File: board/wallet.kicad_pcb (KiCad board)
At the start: 4 copper layers, 48 x 85 mm, 108 parts, among them J1 TYPE-C-31-M-12, U1 BQ25185DLHR, U11 E73-2G4M08S1C, U12 ME6211C28M5G-N, U13 TPS60230RGTR, U14 TLV70313DBVR, U15 MAX17048G+T10, U2 TPS63802DLAR, U4 STM32U585VIT6Q, U5 SE050E2HQ1/Z01Z3Z, U6 TS3USB221ARSER, U7 SN74LVC1G02DBVR(UMW), U8 TPS22917DBVR, U9 TXU0202DCUR

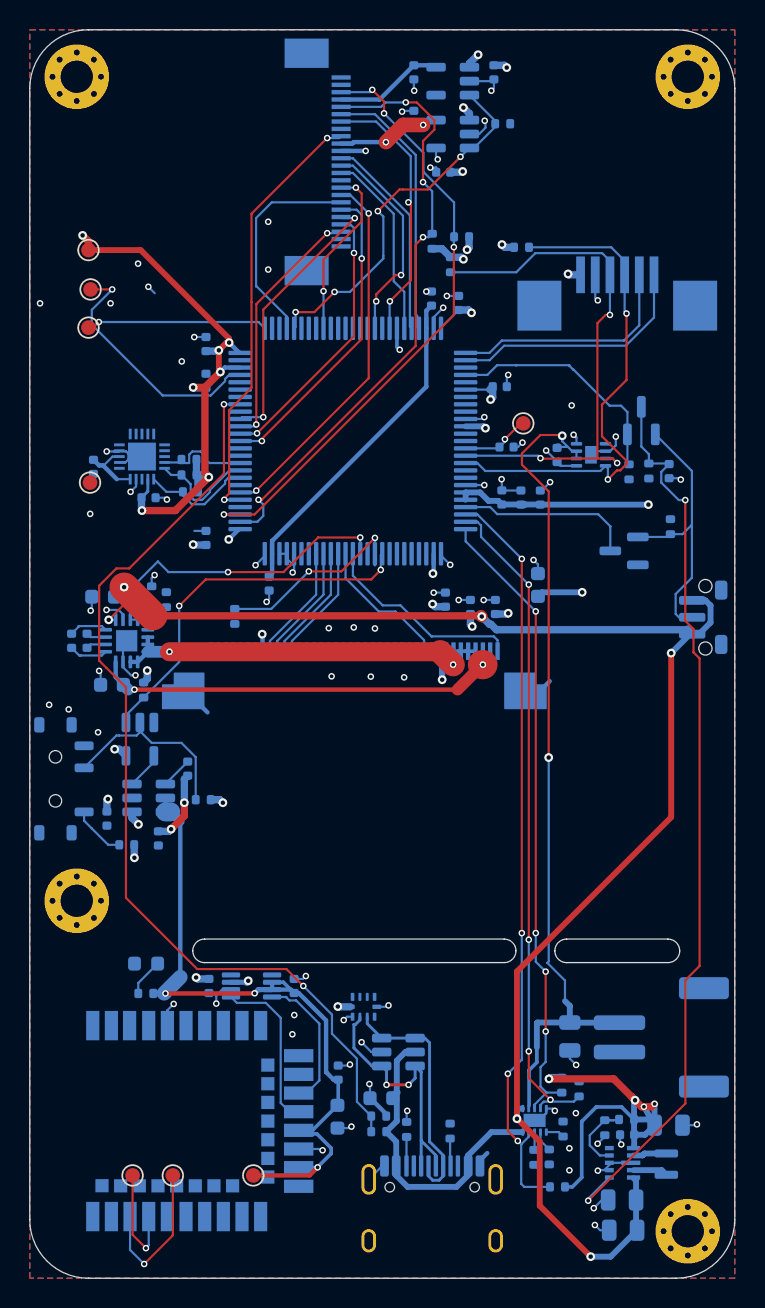
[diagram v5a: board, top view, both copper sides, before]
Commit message: Owner: radio RX routed, camera I2C pull-ups moved north, CAM_SCL re-routed
Hand work: RADIO_RXD_MCU routed (40 mm, back copper); R_CSCL moved up beside
the camera supply output (C_AVOUT turned 180 to make room), R_CSDA 1.3 mm
north, CAM_SCL redrawn to the new pull-up; small reroutes of CAM_D1, CAM_EN,
CAM_XCLK, CAM_AVDD, RADIO_3V3, V3V3, AIRGAP_SENSE; 8 GND vias.

As committed: 7 unconnected (USB MCU pair, RADIO_TXD, AIRGAP x2, J_TFT pin 40
GND now cut off from the pour), 3 vias that connect one layer only (CAM_EN,
CAM_D1, CAM_XCLK, each in the middle of a single-layer track) and 3 CAM_SCL
crumbs. Cleaned up in the next commit.

Co-Authored-By: Claude Opus 5.5 <noreply@anthropic.com>
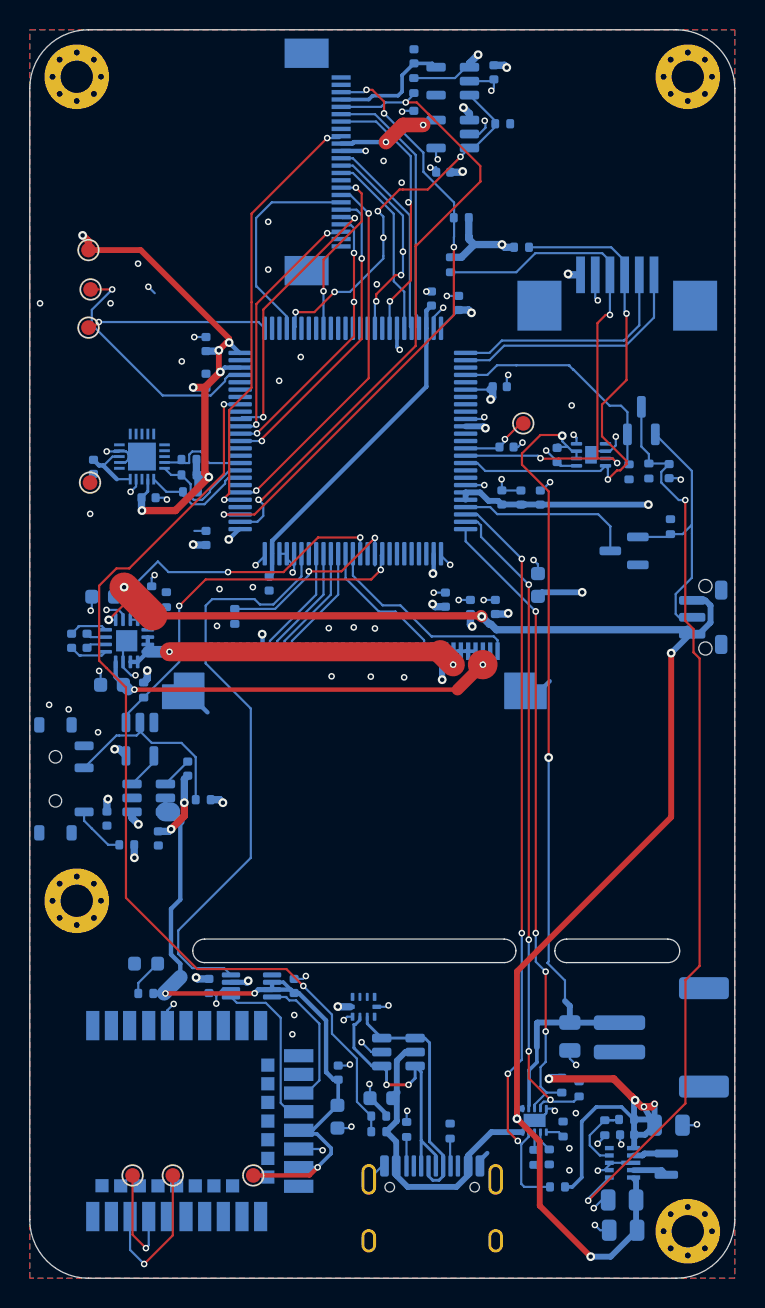
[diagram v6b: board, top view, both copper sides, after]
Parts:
- moved R_CSCL 10.7 mm to (26.1, 3.80), turned to 90 degrees
- moved R_CSDA 1.30 mm to (29.4, 12.8)
- moved C_AVOUT 1.09 mm to (26.2, 1.81), turned to 90 degrees
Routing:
- net RADIO_RXD_MCU: track 0.00 -> 40.4 mm
- net V3V3: track 128.2 -> 135.2 mm, vias 44 -> 42
- net CAM_SCL: track 41.6 -> 45.1 mm, vias 4 -> 2
- net GND: track 85.2 -> 83.5 mm, vias 80 -> 86
- net CAM_AVDD: track 7.48 -> 8.42 mm
- net RADIO_3V3: track 48.8 -> 49.3 mm
- net CAM_EN: vias 4 -> 5
- net CAM_XCLK: vias 2 -> 3
- net CAM_D1: vias 2 -> 3

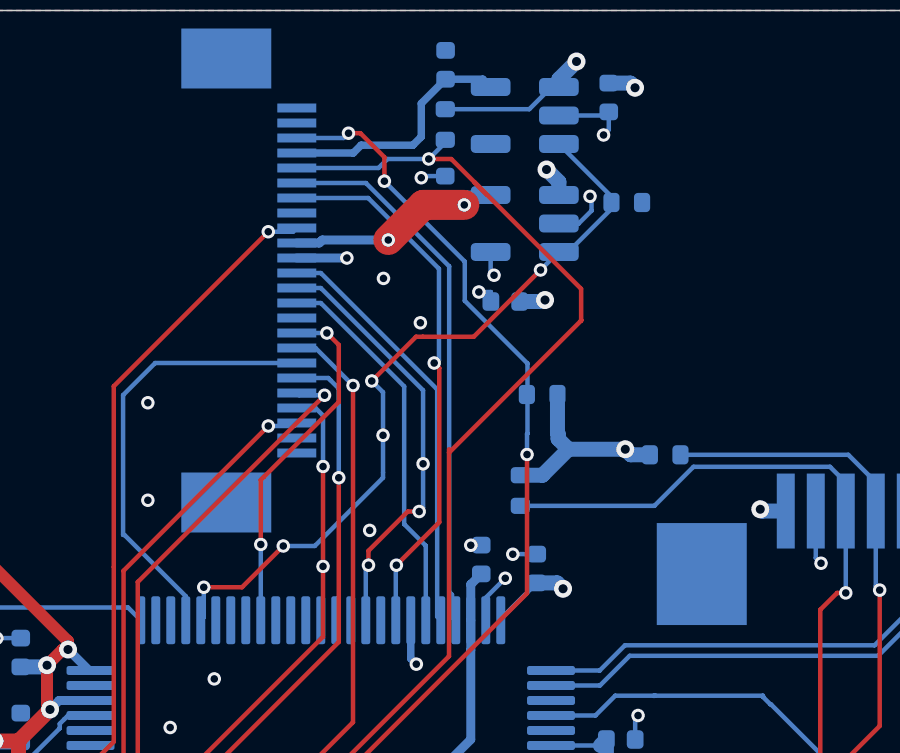
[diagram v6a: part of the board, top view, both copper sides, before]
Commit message: USB MCU pair named as a differential pair; owner's leftover vias and stubs out
USB_DP_MCU/USB_DN_MCU -> USB_MCU_DP/USB_MCU_DN: a name ending in P/N is what
KiCad's Route Differential Pair and humanRouter's pair detection both key on
(USB_DP/USB_DN already did). Renamed in the tscircuit source, the MCU and pin
maps, the net class pattern and the board; nets, AF, sync and pin-table gates pass.

cleanCopper also removes, on a net that is complete: a via that joins one
layer only (left mid-track after a reroute) and a dangling stub under 1 mm.
Nets still waiting for routing keep their fanouts. Removed: the CAM_EN, CAM_D1
and CAM_XCLK mid-track vias and three CAM_SCL stubs/crumbs; unconnected
unchanged (7).

Co-Authored-By: Claude Opus 5.5 <noreply@anthropic.com>
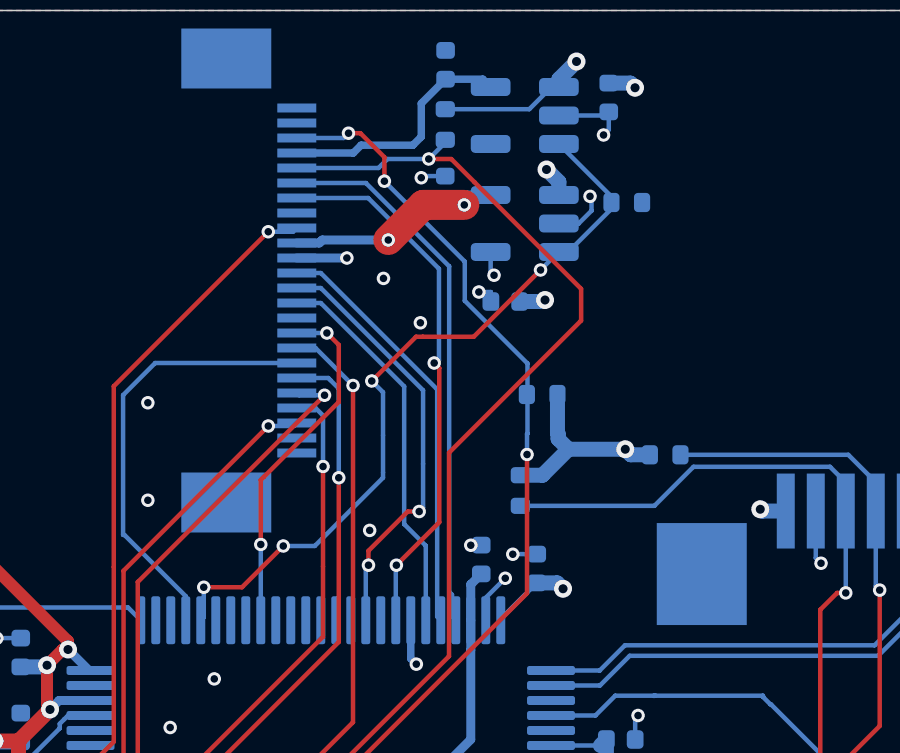
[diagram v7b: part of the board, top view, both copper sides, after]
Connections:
- net USB_DN_MCU renamed USB_MCU_DN
- net USB_DP_MCU renamed USB_MCU_DP
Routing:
- net CAM_SCL: track 45.1 -> 44.3 mm
- net CAM_XCLK: vias 3 -> 2
- net CAM_EN: vias 5 -> 4
- net CAM_D1: vias 3 -> 2
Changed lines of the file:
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@@
 			(layers "B.Cu" "B.Mask" "B.Paste")
 			(roundrect_rratio 0.25)
-			(net "USB_DN_MCU")
+			(net "USB_MCU_DN")
 		)
 		(pad "71" smd roundrect
@@
 			(layers "B.Cu" "B.Mask" "B.Paste")
 			(roundrect_rratio 0.25)
-			(net "USB_DP_MCU")
+			(net "USB_MCU_DP")
 		)
 		(pad "72" smd roundrect
@@
 			(layers "B.Cu" "B.Mask" "B.Paste")
 			(roundrect_rratio 0.2)
-			(net "USB_DP_MCU")
+			(net "USB_MCU_DP")
 		)
 		(pad "2" smd roundrect
@@
 			(layers "B.Cu" "B.Mask" "B.Paste")
 			(roundrect_rratio 0.25)
-			(net "USB_DN_MCU")
+			(net "USB_MCU_DN")
 		)
 		(pad "3" smd roundrect
@@
 		(net "CAM_EN")
 	)
-	(via
-		(at 24.075 14.16)
-		(size 0.45)
-		(drill 0.25)
-		(layers "F.Cu" "B.Cu")
-		(net "CAM_EN")
-	)
 	(segment
 		(start 31.69 6.61)
@@
 	)
 	(segment
-		(start 26.275 14.74)
-		(end 26.275 14.625)
-		(width 0.15)
-		(layer "F.Cu")
-		(net "CAM_SCL")
-	)
-	(segment
 		(start 26.35 4.95)
 		(end 25.6 4.95)
@@
 	)
 	(segment
-		(start 30.6775 10.3375)
-		(end 30.69 10.325)
-		(width 0.15)
-		(layer "F.Cu")
-		(net "CAM_SCL")
-	)
-	(segment
 		(start 30.6775 9.2775)
 		(end 27.125 5.725)
@@
 	)
 	(segment
-		(start 27.55 6.15)
-		(end 27.125 5.725)
-		(width 0.15)
-		(layer "F.Cu")
-		(net "CAM_SCL")
-	)
-	(segment
 		(start 30.6775 10.3375)
 		(end 30.6775 9.2775)
@@
 	)
 	(via
-		(at 22.075 18.53)
-		(size 0.45)
-		(drill 0.25)
-		(layers "F.Cu" "B.Cu")
-		(net "CAM_D1")
-	)
-	(via
 		(at 22.075 15.2)
 		(size 0.45)
@@
 		(size 0.45)
 		(drill 0.25)
-		(layers "F.Cu" "B.Cu")
-		(net "CAM_XCLK")
-	)
-	(via
-		(at 25.41 15.11)
-		(size 0.45)
-		(drill 0.25)

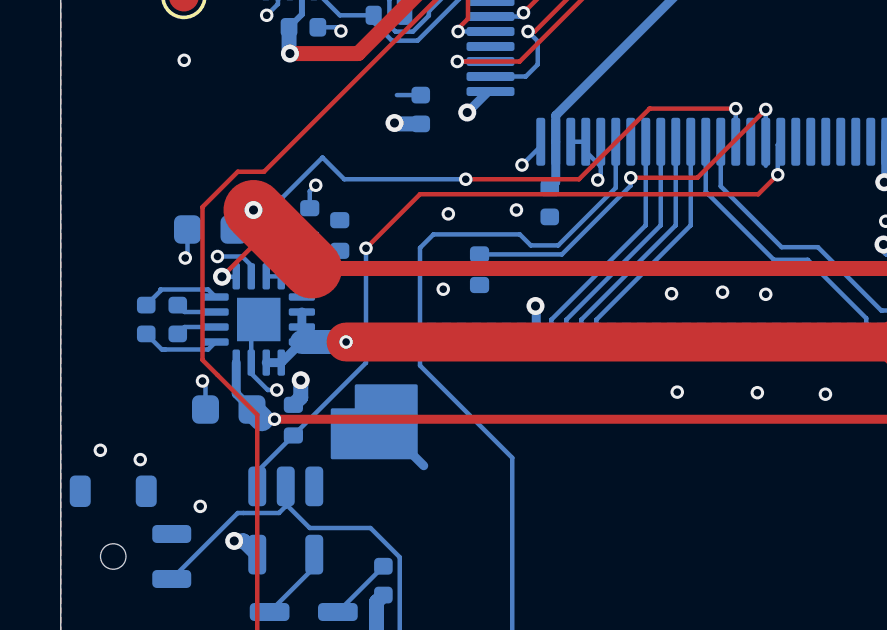
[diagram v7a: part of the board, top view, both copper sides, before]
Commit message: J_TFT pin 40 joined to the GND via above the row; cleanup tools keep their DRC reports out of board/
The RADIO_RXD route sealed the last FPC contact's piece of pour (a 0.3 mm pin
at 0.5 mm pitch takes no thermal spokes there). A 0.2 mm track to the owner's
existing GND via 0.9 mm north joins it, no via beside the pad. Unconnected 7 -> 6.

Co-Authored-By: Claude Opus 5.5 <noreply@anthropic.com>
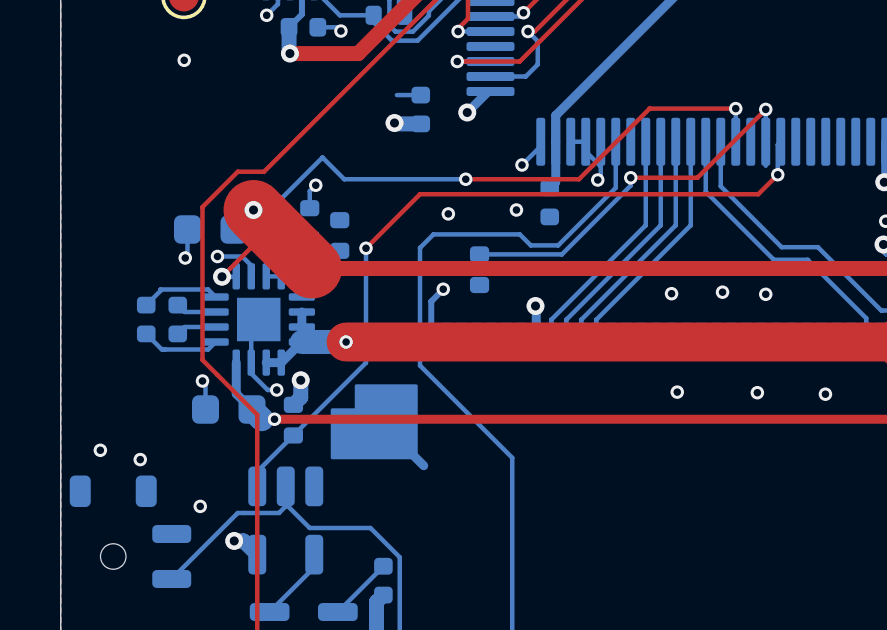
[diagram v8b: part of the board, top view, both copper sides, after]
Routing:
- net GND: track 83.5 -> 85.4 mm
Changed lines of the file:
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@@
+	)
+	(segment
+		(start 12.35 41)
+		(end 12.75 40.59)
+		(width 0.2)
+		(layer "B.Cu")
+		(net "GND")
 	)
 	(segment
@@
 		(layer "B.Cu")
 		(net "GND")
+	)
+	(segment
+		(start 12.35 42.31)
+		(end 12.35 41)
+		(width 0.2)
+		(layer "B.Cu")
+		(net "GND")
